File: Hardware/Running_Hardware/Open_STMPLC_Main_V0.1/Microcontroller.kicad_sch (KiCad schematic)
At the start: 73 parts, among them J1 Conn_02x08_Odd_Even, J12 USB C, J2 USB C, J3 Conn_01x04, SW1 Switch_6x6, U1 STM32F407IGTx, U3 TPS3430WDRC, U4 CH340C, Y1 48MHz, Y2 32.768kHz

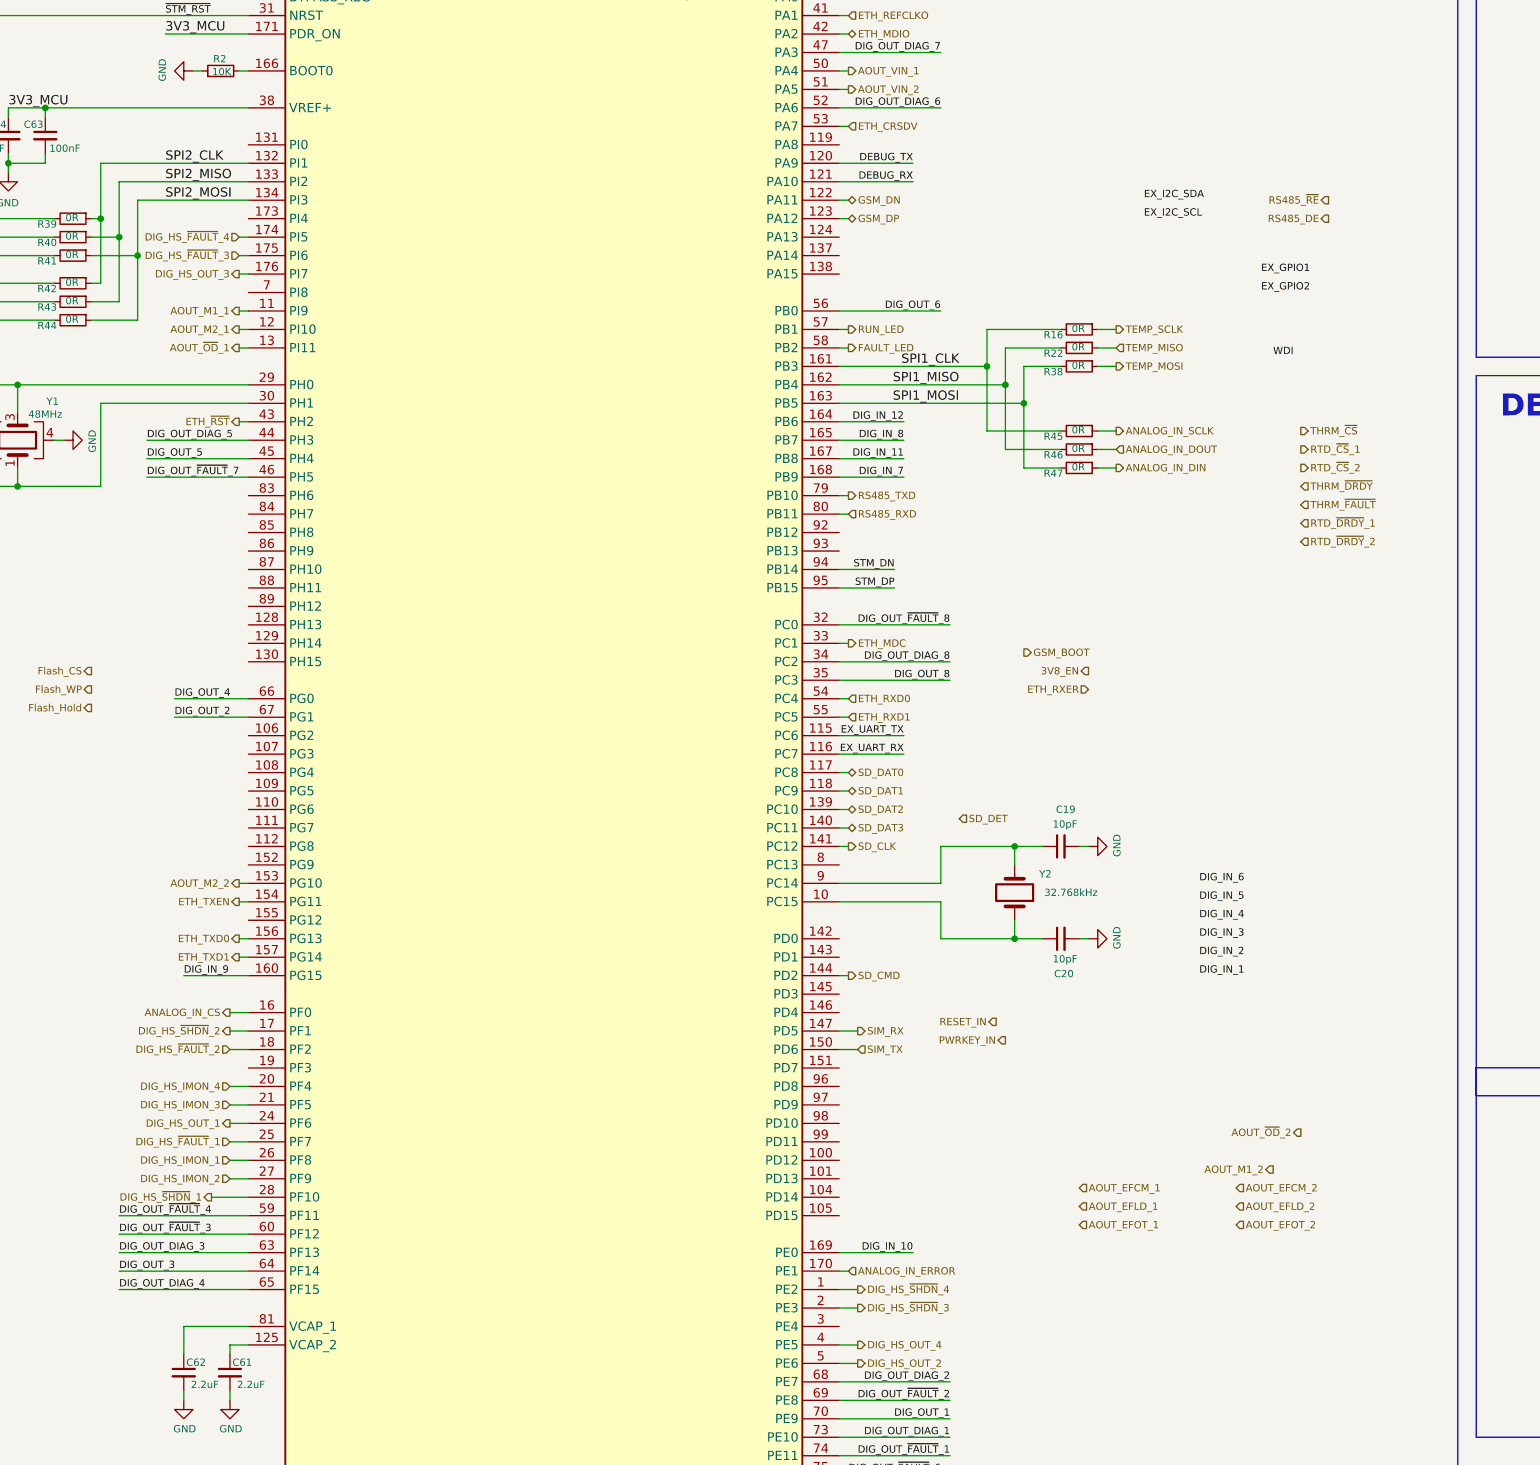
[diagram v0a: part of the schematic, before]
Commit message: MCU Pin mapping
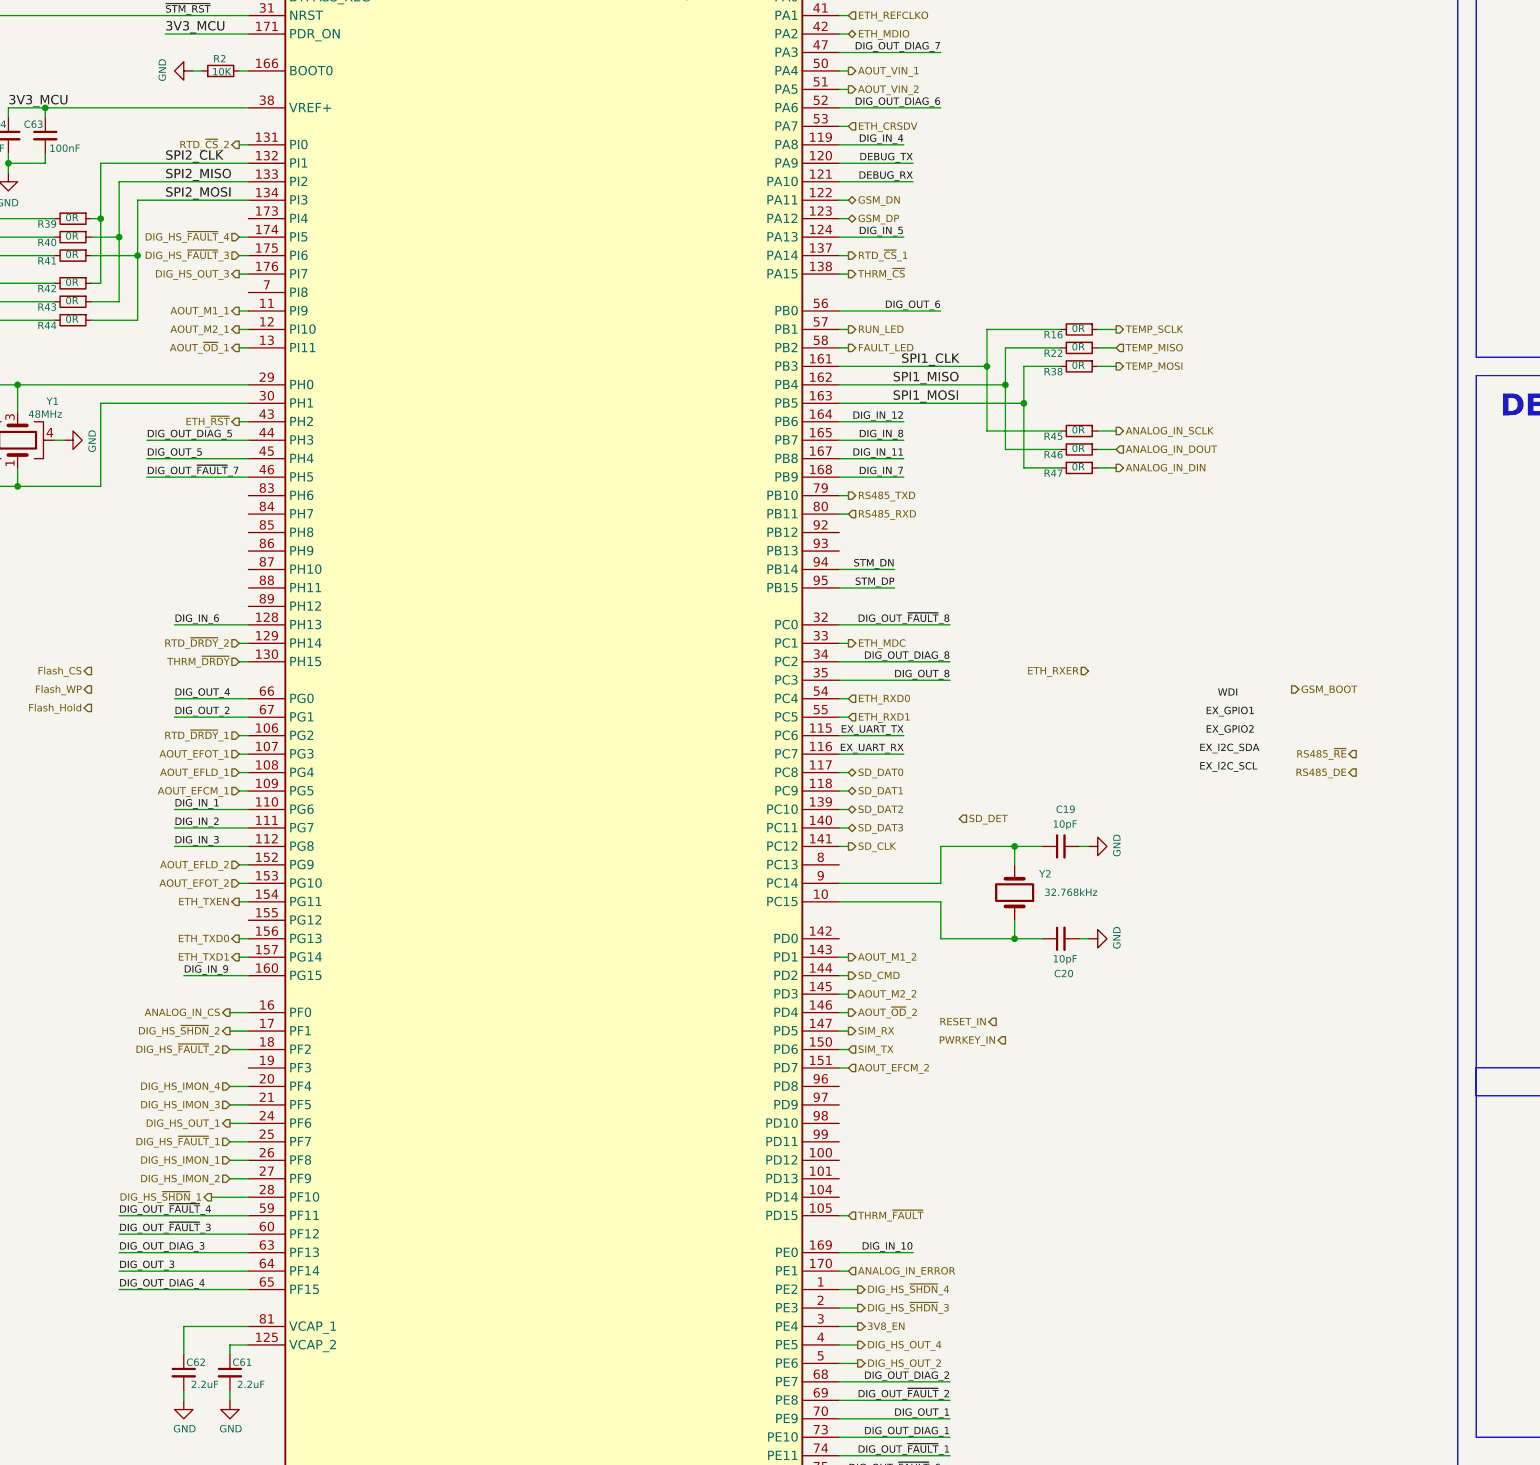
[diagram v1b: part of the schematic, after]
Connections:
- net 3V8_EN: now also U1.3 (PE4)
- net AOUT_EFCM_1: now also U1.109 (PG5)
- net AOUT_EFCM_2: now also U1.151 (PD7)
- net AOUT_EFLD_1: now also U1.108 (PG4)
- net AOUT_EFLD_2: now also U1.152 (PG9)
- net AOUT_EFOT_1: now also U1.107 (PG3)
- net AOUT_EFOT_2: now also U1.153 (PG10)
- net AOUT_M1_2: now also U1.143 (PD1)
- net AOUT_M2_2: now also U1.145 (PD3); no longer U1.153 (PG10)
- net AOUT_~{OD}_2: now also U1.146 (PD4)
- net DIG_IN_1: now also U1.110 (PG6)
- net DIG_IN_2: now also U1.111 (PG7)
- net DIG_IN_3: now also U1.112 (PG8)
- net DIG_IN_4: now also U1.119 (PA8)
- net DIG_IN_5: now also U1.124 (PA13)
- net DIG_IN_6: now also U1.128 (PH13)
- net RTD_~{CS}_1: now also U1.137 (PA14)
- net RTD_~{CS}_2: now also U1.131 (PI0)
- net RTD_~{DRDY}_1: now also U1.106 (PG2)
- net RTD_~{DRDY}_2: now also U1.129 (PH14)
- net THRM_~{CS}: now also U1.138 (PA15)
- net THRM_~{DRDY}: now also U1.130 (PH15)
- net THRM_~{FAULT}: now also U1.105 (PD15)

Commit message: PCB routing completion v0.1 Main
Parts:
- removed R17, R30: 10K, Resistor_SMD:R_0603_1608Metric_Pad0.98x0.95mm_HandSolder, symbol Device:R_Small
- added D14, D15, D16, D17, D18, D20, D21, D22, D23, D24, D25, D26, D27, D28, D29, D30, D31: UAD8C05L01, Diode_SMD:D_SOD-882, symbol Device:D_TVS_Small
- added R50, R51, R52, R53: 4.7K, Resistor_SMD:R_0603_1608Metric_Pad0.98x0.95mm_HandSolder, symbol Device:R_Small
- added U11, U12: SRV05-4, Package_TO_SOT_SMD:SOT-23-6, symbol Power_Protection:SRV05-4
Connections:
- net +3V3: now also D14.2 (A2), D29.2 (A2), R50.2, R51.2, R52.2, R53.2; no longer J1.2 (Pin_2)
- net +5V: now also J1.2 (Pin_2), D28.2 (A2)
- net DEBUG_DN: now also U11.1 (IO1)
- net DEBUG_DP: now also U11.3 (IO2)
- net DIG_OUT_5: now also U1.86 (PH9); no longer U1.45 (PH4)
- net DIG_OUT_~{FAULT}_7: now also U1.83 (PH6); no longer U1.46 (PH5)
- net DISP_SCL: now also U1.84 (PH7), D31.2 (A2), R51.1
- net DISP_SDA: now also U1.85 (PH8), D30.2 (A2), R50.1
- net EX_GPIO1: now also U1.93 (PB13), D24.2 (A2)
- net EX_GPIO2: now also J1.7 (Pin_7), U1.92 (PB12), D17.2 (A2); no longer J1.12 (Pin_12)
- net EX_I2C_SCL: now also J1.3 (Pin_3), U1.45 (PH4), D15.2 (A2), R52.1; no longer J1.5 (Pin_5)
- net EX_I2C_SDA: now also J1.4 (Pin_4), U1.46 (PH5), D27.2 (A2), R53.1; no longer J1.3 (Pin_3)
- net EX_SPI_CLK: now also J1.12 (Pin_12), D23.2 (A2); no longer J1.11 (Pin_11)
- net EX_SPI_MISO: now also J1.11 (Pin_11), D20.2 (A2); no longer J1.9 (Pin_9)
- net EX_SPI_MOSI: now also J1.9 (Pin_9), D18.2 (A2); no longer J1.7 (Pin_7)
- net EX_UART_RX: now also J1.13 (Pin_13), D21.2 (A2); no longer J1.8 (Pin_8)
- net EX_UART_TX: now also J1.14 (Pin_14), D22.2 (A2); no longer J1.6 (Pin_6)
- net Flash_CS: now also U1.97 (PD9)
- net Flash_Hold: now also U1.96 (PD8)
- net Flash_WP: now also U1.98 (PD10)
- net GND: now also D14.1 (A1), D15.1 (A1), D16.1 (A1), D17.1 (A1), D18.1 (A1), D20.1 (A1), D21.1 (A1), D22.1 (A1), D23.1 (A1), D24.1 (A1), D25.1 (A1), D26.1 (A1), D27.1 (A1), D28.1 (A1), D29.1 (A1), D30.1 (A1), D31.1 (A1), U11.2 (VN), U12.2 (VN)
- net GSM_BOOT: now also U1.99 (PD11)
- net PWRKEY_IN: now also U1.101 (PD13)
- net RESET_IN: now also U1.100 (PD12)
- net RS485_DE: now also U1.77 (PE14)
- net RS485_~{RE}: now also U1.78 (PE15)
- net SD_DET: now also U1.104 (PD14)
- net STM_DN: now also U12.1 (IO1)
- net STM_DP: now also U12.3 (IO2)
- net WDI: now also U1.7 (PI8)
- net VBUS: now reaches J2.A4 (VBUS), J2.A9 (VBUS), J2.B4 (VBUS), J2.B9 (VBUS), R9.1
- net VBUS: now also J12.A4 (VBUS), J12.A9 (VBUS), J12.B4 (VBUS), J12.B9 (VBUS), R32.1, U11.5 (VP), U12.5 (VP)
- net EX_GPIO5: now reaches U1.87 (PH10)
- net EX_GPIO5: now also J1.6 (Pin_6), D26.2 (A2)
- net EX_GPIO4: now reaches U1.88 (PH11)
- net EX_GPIO4: now also J1.5 (Pin_5), D16.2 (A2)
- net EX_GPIO3: now reaches U1.89 (PH12)
- net EX_GPIO3: now also J1.8 (Pin_8), D25.2 (A2)
- no-connect marks 14 -> 17
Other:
- moved on the sheet: BT1, C1, C10, C11, C12, C13, C14, C16, C18, C19, C2, C20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

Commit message: Silkscreen and DRC
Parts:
- added J11: Conn_01x05, Connector_PinHeader_2.54mm:PinHeader_1x05_P2.54mm_Vertical, symbol Connector_Generic:Conn_01x05
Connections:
- net 3V3_MCU: now also J11.5 (Pin_5)
- net DIG_IN_5: now also U1.173 (PI4); no longer U1.124 (PA13)
- net GND: now also J11.3 (Pin_3)
- net RTD_~{CS}_1: now also U1.142 (PD0); no longer U1.137 (PA14)
- net ~{STM_RST}: now also J11.1 (Pin_1)
- new net SWCLK: J11.4 (Pin_4), U1.137 (PA14)
- new net SWDIO: J11.2 (Pin_2), U1.124 (PA13)

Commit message: Gerber generation v0.1
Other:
- company: (none) -> Thingslista Automation LLP
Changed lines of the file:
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@@
 	(title_block
 		(title "Open_STMPLC_Main")
-		(date "2026-05-24")
+		(date "2026-06-03")
 		(rev "0.1")
+		(company "Thingslista Automation LLP")
 	)
 	(rectangle
